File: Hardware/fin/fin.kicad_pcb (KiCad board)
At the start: 2 copper layers, 152.4 x 63.5 mm, 34 parts, among them J1 Conn_01x10_Pin, J2 Conn_01x04_Pin, J3 Conn_01x04_Pin, J5 Conn_01x04_Pin, U1 ADS131M03QPWRQ1, U2 STM32L412C8Tx, U3 W25N512GVEIG, U4 TMP235A4DBZR

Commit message: really scuffed draft
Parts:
- removed D1, D4: LED, LED_SMD:LED_0603_1608Metric
- removed R10, R7: 220, Resistor_SMD:R_0603_1608Metric
- C3, R13, R14, R3, R4: moved to F.Cu
- U1: moved to B.Cu
- moved R14 8.17 mm to (121.2, 143.5), turned to 180 degrees
- moved C3 4.00 mm to (115.0, 144.5)
- moved C11 2.50 mm to (113.0, 142.5)
- moved R3 1.17 mm to (117.7, 145.5), turned to 180 degrees
- moved R4 1.17 mm to (117.7, 143.5), turned to 0 degrees
- moved R13 0.30 mm to (116.2, 141.5), turned to 0 degrees
- turned C9 to 180 degrees
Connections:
- J1 pad 3: QSPI_IO1 -> QSPI_IO2
- J1 pad 4: QSPI_IO2 -> QSPI_IO1
- J1 pad 7: SWDIO -> SWCLK
- J1 pad 8: SWCLK -> SWDIO
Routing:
- net +3.3V: track 0.00 -> 211.6 mm, vias 0 -> 10
- net GND: track 0.00 -> 85.0 mm, vias 0 -> 20
- net GAUGE2_IN_P: track 0.00 -> 75.3 mm, vias 0 -> 1
- net SWDIO: track 0.00 -> 67.2 mm
- net SWCLK: track 0.00 -> 59.3 mm
- net SIGNAL: track 0.00 -> 54.4 mm
- net QSPI_IO1: track 0.00 -> 54.2 mm, vias 0 -> 2
- net ~{FLASH_CS}: track 0.00 -> 51.4 mm
- net AVBAY_SYNC: track 0.00 -> 51.0 mm
- net QSPI_IO3: track 0.00 -> 50.8 mm
- net QSPI_IO2: track 0.00 -> 46.0 mm, vias 0 -> 2
- net QSPI_IO0: track 0.00 -> 42.8 mm, vias 0 -> 2
- net QSPI_SCK: track 0.00 -> 35.6 mm
- net GAUGE1_IN_P: track 0.00 -> 32.3 mm
- net ADC_~{SYNC}/~{RST}: track 0.00 -> 22.3 mm, vias 0 -> 1
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- added copper zone on B.Cu, net GND
- added copper zone on F.Cu, net GND

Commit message: updated fin schem
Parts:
- removed C6, C7, C8, C9: 100nF, Capacitor_SMD:C_0603_1608Metric
- removed U2: STM32L412C8Tx, Package_QFP:LQFP-48_7x7mm_P0.5mm
- added C13: 100nF, Capacitor_SMD:C_0603_1608Metric, F.Cu at (95.5, 120.8)
- added C14: 100nF, Capacitor_SMD:C_0603_1608Metric, F.Cu at (95.5, 123.3)
- added C15: 100nF, Capacitor_SMD:C_0603_1608Metric, F.Cu at (95.5, 125.8)
- added C16: 100nF, Capacitor_SMD:C_0603_1608Metric, F.Cu at (95.5, 128.3)
- added D1: LED, LED_SMD:LED_0603_1608Metric, F.Cu at (99.6, 128.1)
- added D4: LED, LED_SMD:LED_0603_1608Metric, F.Cu at (99.6, 130.7)
- added R10: 220, Resistor_SMD:R_0603_1608Metric, F.Cu at (95.5, 133.3)
- added R7: 220, Resistor_SMD:R_0603_1608Metric, F.Cu at (95.5, 130.8)
- added U5: STM32L412K8Ux, Package_DFN_QFN:QFN-32-1EP_5x5mm_P0.5mm_EP3.45x3.45mm, F.Cu at (99.2, 145.8)
- moved U3 1.58 mm to (84.0, 145.5)
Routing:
- net +3.3V: track 211.6 -> 0.00 mm, vias 10 -> 0
- net GND: track 85.0 -> 0.00 mm, vias 20 -> 0
- net GAUGE2_IN_P: track 75.3 -> 0.00 mm, vias 1 -> 0
- net SWDIO: track 67.2 -> 0.00 mm
- net SWCLK: track 59.3 -> 0.00 mm
- net SIGNAL: track 54.4 -> 0.00 mm
- net QSPI_IO1: track 54.2 -> 0.00 mm, vias 2 -> 0
- net ~{FLASH_CS}: track 51.4 -> 0.00 mm
- net AVBAY_SYNC: track 51.0 -> 0.00 mm
- net QSPI_IO3: track 50.8 -> 0.00 mm
- net QSPI_IO2: track 46.0 -> 0.00 mm, vias 2 -> 0
- net QSPI_IO0: track 42.8 -> 0.00 mm, vias 2 -> 0
- net QSPI_SCK: track 35.6 -> 0.00 mm
- net GAUGE1_IN_P: track 32.3 -> 0.00 mm
- net ADC_~{SYNC}/~{RST}: track 22.3 -> 0.00 mm, vias 1 -> 0
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
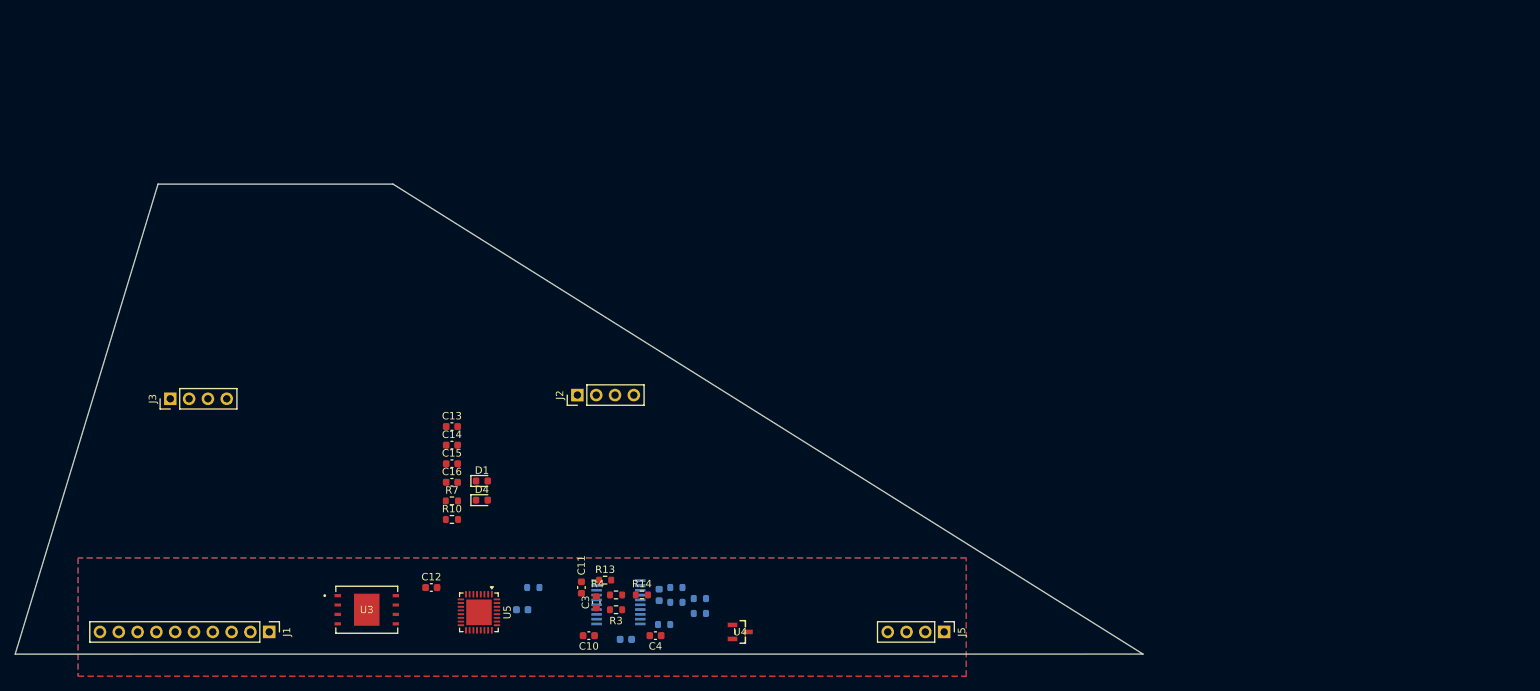
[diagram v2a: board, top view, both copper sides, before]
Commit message: accelerometers, coupled flash layout
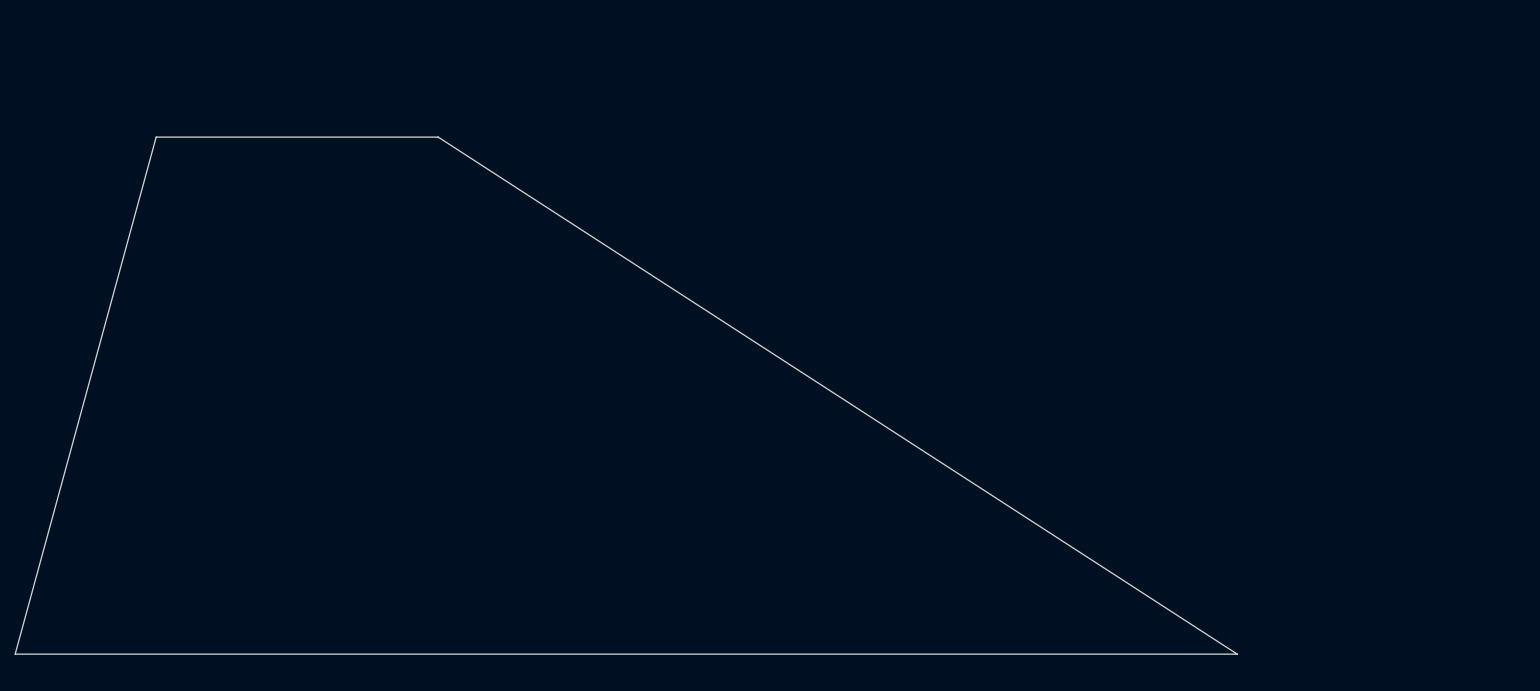
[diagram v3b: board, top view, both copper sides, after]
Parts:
- removed C1, C3, C5: 10 nF, Capacitor_SMD:C_0603_1608Metric
- removed C10, C4: 1 uF, Capacitor_SMD:C_0603_1608Metric
- removed C11: 220 nF, Capacitor_SMD:C_0603_1608Metric
- removed C12, C13, C14, C15, C16, C2: 100nF, Capacitor_SMD:C_0603_1608Metric
- removed D1, D4: LED, LED_SMD:LED_0603_1608Metric
- removed J1: Conn_01x10_Pin, Connector_PinHeader_2.54mm:PinHeader_1x10_P2.54mm_Vertical
- removed J2, J3, J5: Conn_01x04_Pin, Connector_PinHeader_2.54mm:PinHeader_1x04_P2.54mm_Vertical
- removed R1: 10 k, Resistor_SMD:R_0603_1608Metric
- removed R10, R7: 220, Resistor_SMD:R_0603_1608Metric
- removed R11, R12, R13, R14: 1 k, Resistor_SMD:R_0603_1608Metric
- removed R2: 5K, Resistor_SMD:R_0603_1608Metric
- removed R3, R4, R5, R6: 2.5 k, Resistor_SMD:R_0603_1608Metric
- removed U1: ADS131M03QPWRQ1, FinLib:ADS131M03
- removed U3: W25N512GVEIG, FinLib:WSON8_8x6_E_WIN
- removed U4: TMP235A4DBZR, FinLib:TMP235A4DBZR
- removed U5: STM32L412K8Ux, Package_DFN_QFN:QFN-32-1EP_5x5mm_P0.5mm_EP3.45x3.45mm
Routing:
- removed copper zone on B.Cu, net GND
- removed copper zone on F.Cu, net GND
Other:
- board size 152.4 x 63.5 mm -> 165.1 x 69.8 mm

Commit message: oooooooooo we're half way theeerree
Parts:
- added C1: 10 nF, Capacitor_SMD:C_0402_1005Metric, F.Cu at (130.0, 121.5)
- added C10: 1 uF, Capacitor_SMD:C_0402_1005Metric, F.Cu at (132.5, 130.5)
- added C11: 220 nF, Capacitor_SMD:C_0402_1005Metric, F.Cu at (129.5, 132.5)
- added C12: 100nF, Capacitor_SMD:C_0402_1005Metric, F.Cu at (160.0, 119.0)
- added C13: 100nF, Capacitor_SMD:C_0402_1005Metric, F.Cu at (151.0, 131.5)
- added C14: 100nF, Capacitor_SMD:C_0402_1005Metric, F.Cu at (150.0, 131.5)
- added C15: 100nF, Capacitor_SMD:C_0402_1005Metric, F.Cu at (149.0, 131.5)
- added C16: 100nF, Capacitor_SMD:C_0402_1005Metric, F.Cu at (148.0, 131.5)
- added C19: 0.1uF, Capacitor_SMD:C_0402_1005Metric, F.Cu at (109.4, 129.5)
- added C2: 100nF, Capacitor_SMD:C_0402_1005Metric, F.Cu at (149.0, 128.5)
- added C20: 0.1uF, Capacitor_SMD:C_0402_1005Metric, F.Cu at (109.4, 132.0)
- added C21: 1uF, Capacitor_SMD:C_0402_1005Metric, F.Cu at (109.4, 133.0)
- added C22: 0.1uF, Capacitor_SMD:C_0402_1005Metric, F.Cu at (111.0, 87.5)
- added C23: 0.1uF, Capacitor_SMD:C_0402_1005Metric, F.Cu at (112.0, 87.5)
- added C24: 1uF, Capacitor_SMD:C_0402_1005Metric, F.Cu at (113.0, 87.5)
- added C3: 10 nF, Capacitor_SMD:C_0402_1005Metric, F.Cu at (128.0, 121.5)
- added C4: 1 uF, Capacitor_SMD:C_0402_1005Metric, F.Cu at (131.5, 123.0)
- added C5: 10 nF, Capacitor_SMD:C_0402_1005Metric, F.Cu at (126.0, 121.5)
- added D1: LED, LED_SMD:LED_0402_1005Metric, F.Cu at (171.0, 145.0)
- added D4: LED, LED_SMD:LED_0402_1005Metric, F.Cu at (171.0, 147.0)
- added J1: Conn_01x10_Pin, Connector_PinHeader_2.54mm:PinHeader_1x10_P2.54mm_Vertical, F.Cu at (75.5, 133.2)
- added J2: Conn_01x04_Pin, Connector_PinHeader_2.54mm:PinHeader_1x04_P2.54mm_Vertical, F.Cu at (180.4, 149.5)
- added J3: Conn_01x04_Pin, Connector_PinHeader_2.54mm:PinHeader_1x04_P2.54mm_Vertical, F.Cu at (180.8, 143.0)
- added J5: Conn_01x04_Pin, Connector_PinHeader_2.54mm:PinHeader_1x04_P2.54mm_Vertical, F.Cu at (208.7, 133.2)
- added R1: 10 k, Resistor_SMD:R_0402_1005Metric, F.Cu at (130.5, 120.0)
- added R10: 220, Resistor_SMD:R_0402_1005Metric, F.Cu at (174.0, 147.0)
- added R11: 1 k, Resistor_SMD:R_0402_1005Metric, F.Cu at (126.0, 118.0)
- added R12: 1 k, Resistor_SMD:R_0402_1005Metric, F.Cu at (126.0, 117.0)
- added R13: 1 k, Resistor_SMD:R_0402_1005Metric, F.Cu at (128.0, 118.0)
- added R14: 1 k, Resistor_SMD:R_0402_1005Metric, F.Cu at (128.0, 117.0)
- added R2: 5K, Resistor_SMD:R_0402_1005Metric, F.Cu at (145.0, 132.5)
- added R3: 2.5 k, Resistor_SMD:R_0402_1005Metric, F.Cu at (128.5, 120.0)
- added R4: 2.5 k, Resistor_SMD:R_0402_1005Metric, F.Cu at (127.5, 120.0)
- added R5: 2.5 k, Resistor_SMD:R_0402_1005Metric, F.Cu at (126.5, 120.0)
- added R6: 2.5 k, Resistor_SMD:R_0402_1005Metric, F.Cu at (125.5, 120.0)
- added R7: 220, Resistor_SMD:R_0402_1005Metric, F.Cu at (174.0, 145.0)
- added U1: ADS131M03QPWRQ1, FinLib:ADS131M03, F.Cu at (128.0, 127.5)
- added U2: ADXL380-1BCCZ-RL7, FinLib:CC-14-3_ADI, F.Cu at (112.5, 131.2)
- added U3: W25N512GVEIG, FinLib:WSON8_8x6_E_WIN, F.Cu at (154.0, 121.0)
- added U4: TMP235A4DBZR, FinLib:TMP235A4DBZR, F.Cu at (137.0, 106.0)
- added U5: STM32L412K8Ux, Package_DFN_QFN:QFN-32-1EP_5x5mm_P0.5mm_EP3.45x3.45mm, F.Cu at (144.0, 127.8)
- added U6: ADXL380-1BCCZ-RL7, FinLib:CC-14-3_ADI, F.Cu at (112.5, 84.5)
- added X1: ECS-327TXO-33-TR, FinLib:ECS-327_ECS, F.Cu at (153.9, 129.7)
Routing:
- net SPI1_SCK: track 0.00 -> 84.4 mm, vias 0 -> 4
- net SPI1_MISO: track 0.00 -> 77.9 mm
- net SPI1_MOSI: track 0.00 -> 77.9 mm, vias 0 -> 4
- net +3.3V: track 0.00 -> 75.7 mm
- net ADXL1_CS: track 0.00 -> 67.6 mm, vias 0 -> 4
- net ADXL2_CS: track 0.00 -> 36.2 mm, vias 0 -> 2
- net ~{ADC_CS}: track 0.00 -> 25.3 mm, vias 0 -> 2
- net ADC_~{SYNC}/~{RST}: track 0.00 -> 22.7 mm
- net TIM2_CH1: track 0.00 -> 22.4 mm, vias 0 -> 2
- net ~{ADC_DRDY}: track 0.00 -> 19.8 mm
- net QSPI_IO0: track 0.00 -> 17.5 mm, vias 0 -> 2
- net QSPI_IO3: track 0.00 -> 16.8 mm, vias 0 -> 2
- net TMP_IN_P: track 0.00 -> 15.6 mm
- net ~{FLASH_CS}: track 0.00 -> 10.1 mm
- net QSPI_IO1: track 0.00 -> 10.1 mm
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- added copper zone on B.Cu, net GND
- added copper zone on F.Cu, net GND
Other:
- board outline removed

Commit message: finalish fin
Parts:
- moved J2 109.1 mm to (92.7, 84.5)
- moved J3 64.0 mm to (142.0, 92.1), turned to 180 degrees
- moved R10 24.7 mm to (152.9, 134.1)
- moved D4 21.2 mm to (154.5, 133.7), turned to 90 degrees
- moved R7 19.9 mm to (157.4, 134.1)
- moved D1 19.0 mm to (155.8, 133.7), turned to 90 degrees
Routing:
- net +3.3V: track 75.7 -> 308.2 mm, vias 0 -> 19
- net QSPI_SCK: track 0.00 -> 105.8 mm, vias 0 -> 2
- net GND: track 4.67 -> 97.1 mm, vias 1 -> 32
- net AVBAY_SYNC: track 0.00 -> 79.7 mm, vias 0 -> 3
- net SIGNAL: track 0.00 -> 76.2 mm, vias 0 -> 3
- net QSPI_IO0: track 17.5 -> 92.2 mm, vias 2 -> 4
- net QSPI_IO2: track 9.04 -> 83.3 mm, vias 0 -> 1
- net ~{FLASH_CS}: track 10.1 -> 79.0 mm, vias 0 -> 2
- net QSPI_IO1: track 10.1 -> 78.6 mm, vias 0 -> 1
- net QSPI_IO3: track 16.8 -> 82.3 mm
- net SWCLK: track 0.00 -> 53.7 mm, vias 0 -> 2
- net SWDIO: track 0.00 -> 51.4 mm, vias 0 -> 2
- net GAUGE1_IN_P: track 0.00 -> 49.0 mm, vias 0 -> 1
- net GAUGE2_IN_P: track 0.00 -> 38.3 mm, vias 0 -> 1
- net STATUS_LED: track 0.00 -> 13.3 mm, vias 0 -> 2
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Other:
- board outline added: 165.1 x 69.8 mm

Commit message: final fin layout
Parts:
- moved U4 28.3 mm to (110.5, 96.0)
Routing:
- net GND: track 97.1 -> 51.7 mm, vias 32 -> 27
- net +3.3V: track 308.2 -> 289.3 mm, vias 19 -> 14
- net TMP_IN_P: track 15.6 -> 32.2 mm, vias 0 -> 2
- net Net-(U6-V1P8): track 4.11 -> 6.12 mm
- net GAUGE2_IN_P: track 38.3 -> 39.5 mm
- net ADXL1_CS: track 67.7 -> 66.4 mm

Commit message: added project for panel, fixed cutout to exclude all traces
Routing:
- net ADXL1_CS: track 66.4 -> 78.7 mm
- net +3.3V: track 289.3 -> 298.6 mm
- net GAUGE1_IN_P: track 49.0 -> 56.8 mm
- net TMP_IN_P: track 32.2 -> 38.1 mm
- net GAUGE2_IN_P: track 39.5 -> 42.5 mm

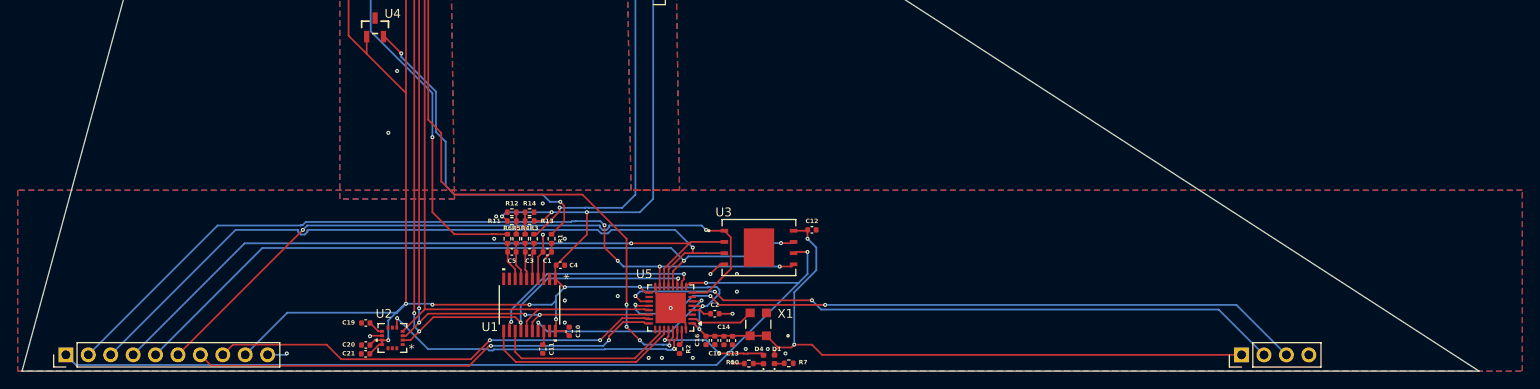
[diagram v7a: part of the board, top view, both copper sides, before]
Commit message: some rerouting and soldermask removing
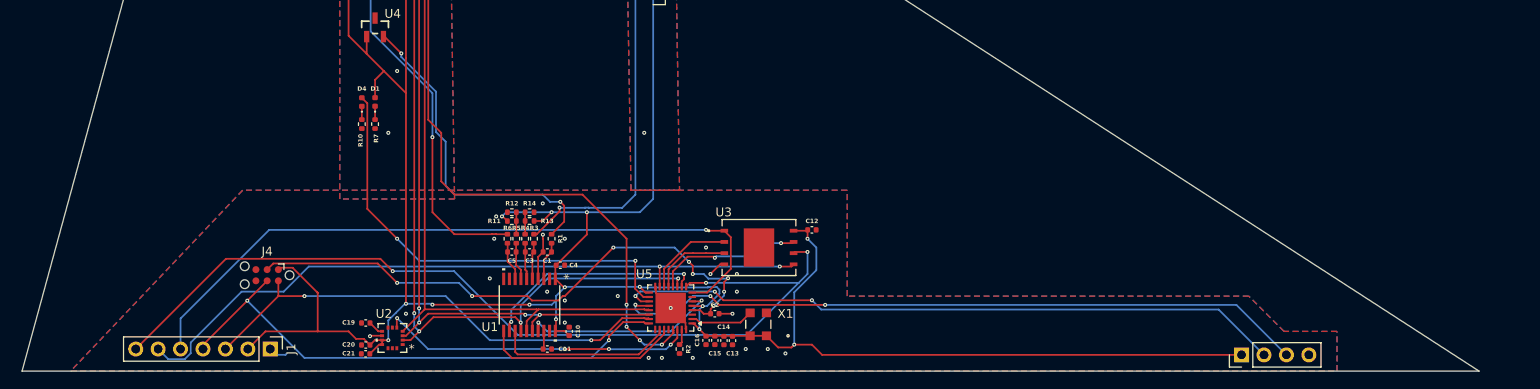
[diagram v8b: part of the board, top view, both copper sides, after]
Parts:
- added J4: Conn_ARM_SWD_TagConnect_TC2030-NL, Connector:Tag-Connect_TC2030-IDC-NL_2x03_P1.27mm_Vertical, F.Cu at (98.3, 124.1)
- C13, C14, C15, C16: value 100nF -> .1uF
- J1: value Conn_01x10_Pin -> Conn_01x07; footprint Connector_PinHeader_2.54mm:PinHeader_1x10_P2.54mm_Vertical -> Connector_PinHeader_2.54mm:PinHeader_1x07_P2.54mm_Vertical
- R2: value 5K -> 10K
- moved R7 54.2 mm to (110.5, 107.0), turned to -90 degrees
- moved D4 54.1 mm to (109.0, 104.5)
- moved D1 53.8 mm to (110.5, 104.5)
- moved R10 51.6 mm to (109.0, 107.0), turned to 90 degrees
- moved J1 23.2 mm to (98.6, 132.5), turned to -90 degrees
- moved C11 0.52 mm to (130.0, 132.5), turned to 0 degrees
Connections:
- net Net-(U5-NRST) renamed ~{RESET}
- J1 pad 1: QSPI_SCK -> GND
- J1 pad 2: QSPI_IO0 -> +3.3V
- J1 pad 3: QSPI_IO2 -> SWDIO
- J1 pad 4: QSPI_IO1 -> SWCLK
- J1 pad 5: QSPI_IO3 -> ~{FLASH_CS}
- J1 pad 6: ~{FLASH_CS} -> QSPI_IO0
- J1 pad 7: SWCLK -> QSPI_SCK
- U5 pad 18: unconnected-(U5-PA8-Pad18) -> STATUS_LED
- U5 pad 28: STATUS_LED -> unconnected-(U5-PB5-Pad28)
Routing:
- net QSPI_IO2: track 83.3 -> 9.04 mm, vias 1 -> 0
- net QSPI_IO1: track 78.6 -> 10.1 mm, vias 1 -> 0
- net QSPI_IO3: track 82.3 -> 16.9 mm
- net ~{RESET}: track 2.25 -> 65.9 mm, vias 0 -> 8
- net STATUS_LED: track 13.3 -> 50.8 mm
- net QSPI_IO0: track 92.2 -> 79.9 mm, vias 4 -> 2
- net SWCLK: track 53.7 -> 61.0 mm
- net +3.3V: track 298.6 -> 305.8 mm
- net SWDIO: track 51.4 -> 55.4 mm
- net QSPI_SCK: track 105.8 -> 103.8 mm, vias 2 -> 3
- net GND: track 51.7 -> 50.3 mm, vias 27 -> 30
- net ADXL2_CS: track 36.5 -> 35.8 mm, vias 2 -> 4
- net ADXL1_CS: track 78.7 -> 78.0 mm
- net ~{FLASH_CS}: track 79.0 -> 79.4 mm, vias 2 -> 1
